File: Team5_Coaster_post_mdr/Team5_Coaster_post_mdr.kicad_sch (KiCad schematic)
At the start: 22 parts, among them J1 XT60, J13 3v3, J2 HC-05, J3 10V, J4 Batt, J5 GND, J6 Vin, SW1 SW_SPDT, U1 PicoW, U2 MC79M15_TO220

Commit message: Working on CDR Motion PCB
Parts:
- added H4: M, MountingHole:MountingHole_4.3mm_M4_Pad_Via, symbol Mechanical:MountingHole_Pad
- added J10, J11, J12, J14, J15: GND, TestPoint:TestPoint_Plated_Hole_D5.0mm, symbol Connector_Generic:Conn_01x01
- added J7: 10V, TestPoint:TestPoint_Plated_Hole_D5.0mm, symbol Connector_Generic:Conn_01x01
- added J8: GPIOs, Connector_PinSocket_2.54mm:PinSocket_1x18_P2.54mm_Vertical, symbol Connector_Generic:Conn_01x18
- added J9: Bluefruit_LE, Connector_PinSocket_2.54mm:PinSocket_1x08_P2.54mm_Vertical, symbol Connector_Generic:Conn_01x08
- D3: footprint LED_SMD:LED_1206_3216Metric -> LED_THT:LED_D3.0mm
- R1: footprint Resistor_SMD:R_1206_3216Metric -> Resistor_THT:R_Axial_DIN0204_L3.6mm_D1.6mm_P7.62mm_Horizontal
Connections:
- net +10V: now also J7.1 (Pin_1)
- net +3V3: now also J9.5 (Pin_5)
- net GND: now also H4.1, J10.1 (Pin_1), J11.1 (Pin_1), J12.1 (Pin_1), J14.1 (Pin_1), J15.1 (Pin_1), J9.7 (Pin_7)
- net DFU: now reaches U1.1 (GPIO0)
- net DFU: now also J8.1 (Pin_1), J9.8 (Pin_8)
- net GPIO7: now reaches U1.10 (GPIO7)
- net GPIO7: now also J8.8 (Pin_8)
- net GPIO8: now reaches U1.11 (GPIO8)
- net GPIO8: now also J8.9 (Pin_9), J9.4 (Pin_4)
- net GPIO9: now reaches U1.12 (GPIO9)
- net GPIO9: now also J8.10 (Pin_10), J9.3 (Pin_3)
- net CTS: now reaches U1.19 (GPIO14)
- net CTS: now also J8.11 (Pin_11), J9.2 (Pin_2)
- net GPIO1: now reaches U1.2 (GPIO1)
- net GPIO1: now also J8.2 (Pin_2), J9.6 (Pin_6)
- net GPIO15: now reaches U1.20 (GPIO15)
- net GPIO15: now also J8.12 (Pin_12), J9.1 (Pin_1)
- net GPIO22: now reaches U1.29 (GPIO22)
- net GPIO22: now also J8.15 (Pin_15)
- net GPIO26: now reaches U1.31 (GPIO26_ADC0)
- net GPIO26: now also J8.16 (Pin_16)
- net GPIO27: now reaches U1.32 (GPIO27_ADC1)
- net GPIO27: now also J8.17 (Pin_17)
- net GPIO28: now reaches U1.34 (GPIO28_ADC2)
- net GPIO28: now also J8.18 (Pin_18)
- net GPIO2: now reaches U1.4 (GPIO2)
- net GPIO2: now also J8.3 (Pin_3)
- net GPIO3: now reaches U1.5 (GPIO3)
- net GPIO3: now also J8.4 (Pin_4)
- net GPIO4: now reaches U1.6 (GPIO4)
- net GPIO4: now also J8.5 (Pin_5)
- net GPIO5: now reaches U1.7 (GPIO5)
- net GPIO5: now also J8.6 (Pin_6)
- net GPIO6: now reaches U1.9 (GPIO6)
- net GPIO6: now also J8.7 (Pin_7)
- net RX renamed GPIO17
- net GPIO17: now also J8.14 (Pin_14)
- net TX renamed GPIO16
- net GPIO16: now also J8.13 (Pin_13)
- no-connect marks 24 -> 8
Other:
- moved on the sheet: J13, J2, J3, J5, U2

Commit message: PCB Read for export, DRC passes
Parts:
- J1: value XT60 -> Vin
- SW1: value SW_SPDT -> Vin_Switch
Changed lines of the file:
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@@
     (in_bom yes) (on_board yes)
     (property "Reference" "J1" (id 0) (at 32.5628 32.385 0))
-    (property "Value" "XT60" (id 1) (at 32.5628 34.6964 0))
+    (property "Value" "Vin" (id 1) (at 30.48 35.56 0))
     (property "Footprint" "Connector_AMASS:AMASS_XT60-M_1x02_P7.20mm_Vertical" (id 2) (at 30.48 40.64 0)
       (effects (font (size 1.27 1.27)) hide)
@@
     (in_bom yes) (on_board yes)
     (property "Reference" "SW1" (id 0) (at 63.5 34.29 0))
-    (property "Value" "SW_SPDT" (id 1) (at 63.5 43.18 0)
+    (property "Value" "Vin_Switch" (id 1) (at 63.5 43.18 0)
       (effects (font (size 1.016 1.016)))
     )
@@
     )
     (path "/00000000-0000-0000-0000-000061de8224"
-      (reference "J1") (unit 1) (value "XT60") (footprint "Connector_AMASS:AMASS_XT60-M_1x02_P7.20mm_Vertical")
+      (reference "J1") (unit 1) (value "Vin") (footprint "Connector_AMASS:AMASS_XT60-M_1x02_P7.20mm_Vertical")
     )
     (path "/7bcc4302-a9ff-46a0-92cd-33fd1db4d7ac"
@@
     )
     (path "/00000000-0000-0000-0000-0000628b996d"
-      (reference "SW1") (unit 1) (value "SW_SPDT") (footprint "Buggy_Footprints:1101M2S3CQE2")
+      (reference "SW1") (unit 1) (value "Vin_Switch") (footprint "Buggy_Footprints:1101M2S3CQE2")
     )
     (path "/d645b5a5-a402-4a08-b2d8-3b05e5bada03"

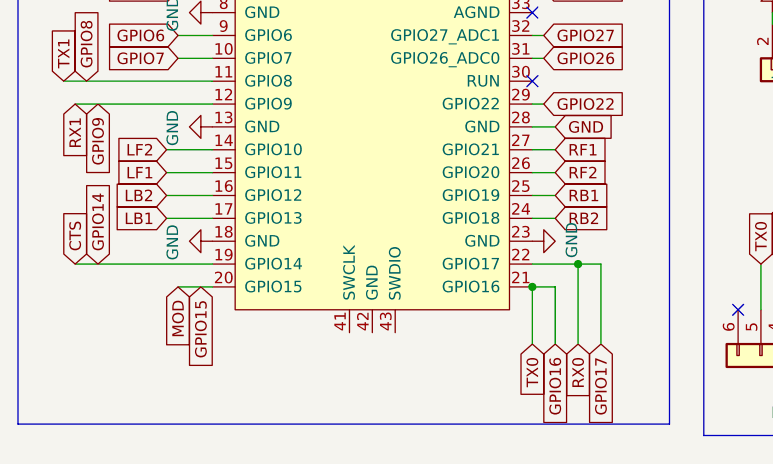
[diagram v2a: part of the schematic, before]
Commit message: Updated Pico Symbol, add some silk screen for gpio
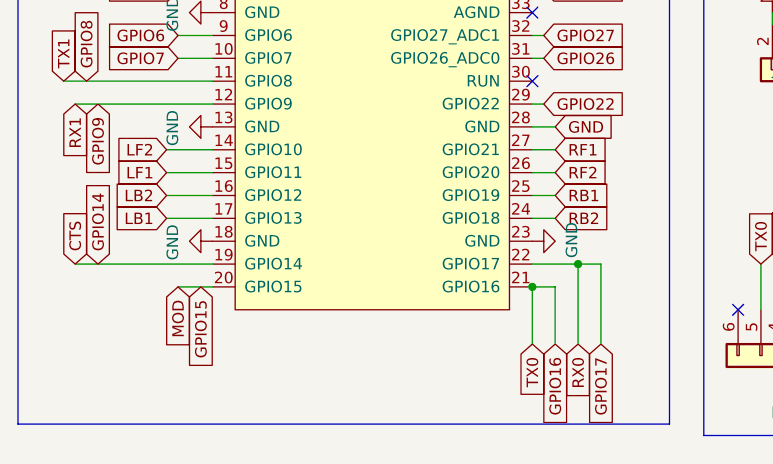
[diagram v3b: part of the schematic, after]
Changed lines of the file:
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@@
     (pin "4")
     (pin "40")
-    (pin "41")
-    (pin "42")
-    (pin "43")
     (pin "5")
     (pin "6")
